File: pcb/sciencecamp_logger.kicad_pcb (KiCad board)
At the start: 2 copper layers, 97 x 46 mm, 29 parts, among them J1 1-Wire, J2 HC-SR04, J3 OLED, J4 Micro_SD_Card_Det, SW1 OFF/ON, SW2 action, U1 74LVC125, U2 AMS1117-3.3

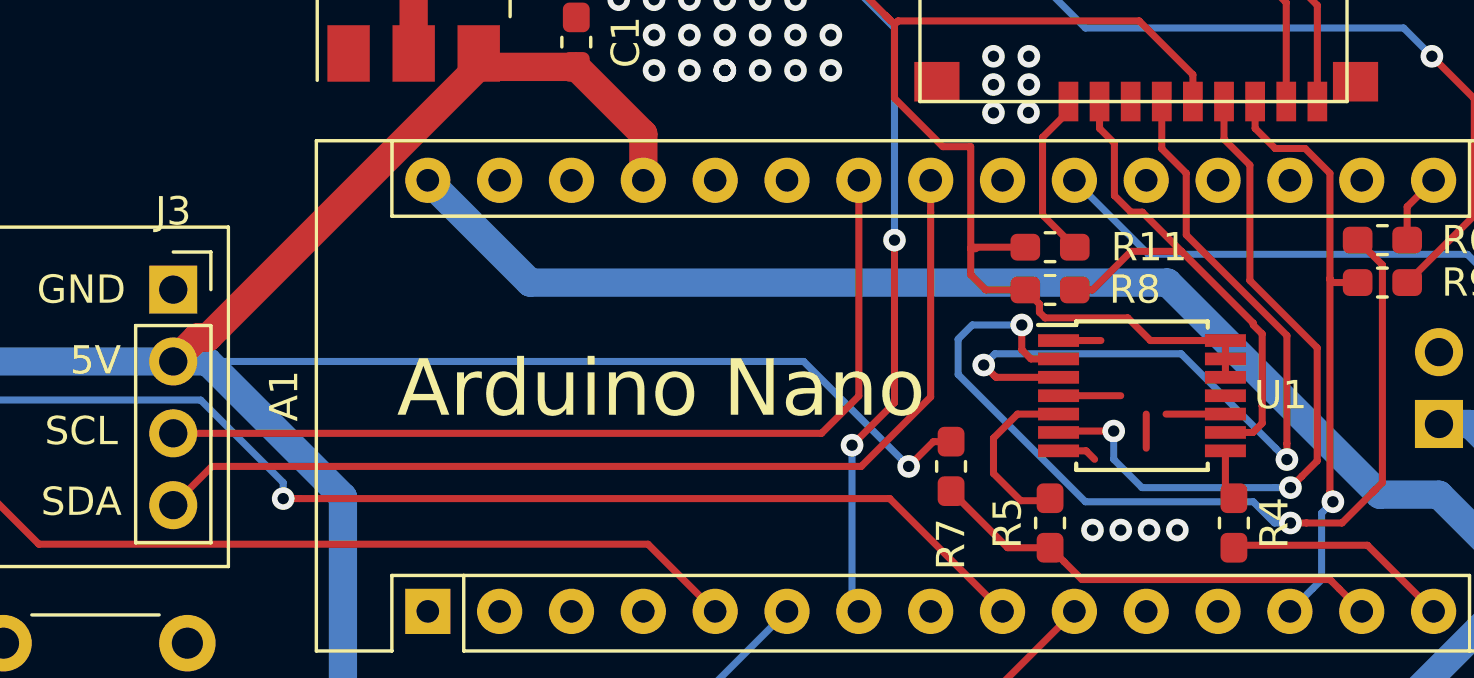
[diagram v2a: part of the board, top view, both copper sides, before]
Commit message: ADD: additional pullups
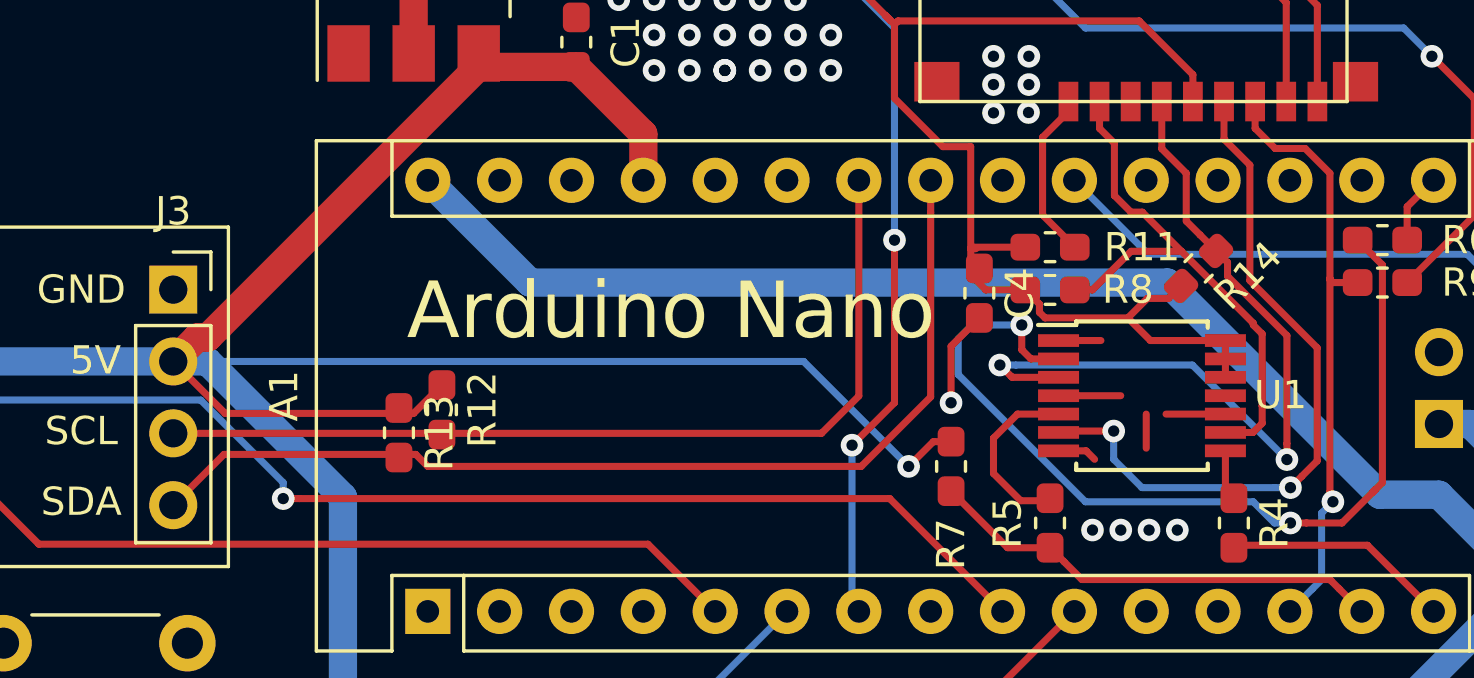
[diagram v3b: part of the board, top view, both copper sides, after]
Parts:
- added C4: 0.1u, Capacitor_SMD:C_0603_1608Metric_Pad1.05x0.95mm_HandSolder, F.Cu at (188.5, 95.4)
- added R12: 2-4k, Resistor_SMD:R_0603_1608Metric_Pad1.05x0.95mm_HandSolder, F.Cu at (169.5, 99.5)
- added R13: 2-4k, Resistor_SMD:R_0603_1608Metric_Pad1.05x0.95mm_HandSolder, F.Cu at (168.0, 100.3)
- added R14: 47k/50k, Resistor_SMD:R_0603_1608Metric_Pad1.05x0.95mm_HandSolder, F.Cu at (196.2, 94.5)
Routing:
- net +5V: track 133.4 -> 144.1 mm
- net GND: track 8.41 -> 11.8 mm, vias 42 -> 43
- net SD_3V3: track 97.8 -> 100.2 mm
- net Net-(J4-Pad5): track 29.8 -> 28.3 mm
